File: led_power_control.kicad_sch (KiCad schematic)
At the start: 16 parts, among them Q2001 BSC110N06NS3GATMA1, Q2002 BSC110N06NS3GATMA1, U2001 BD_2EDN8533FXTMA1

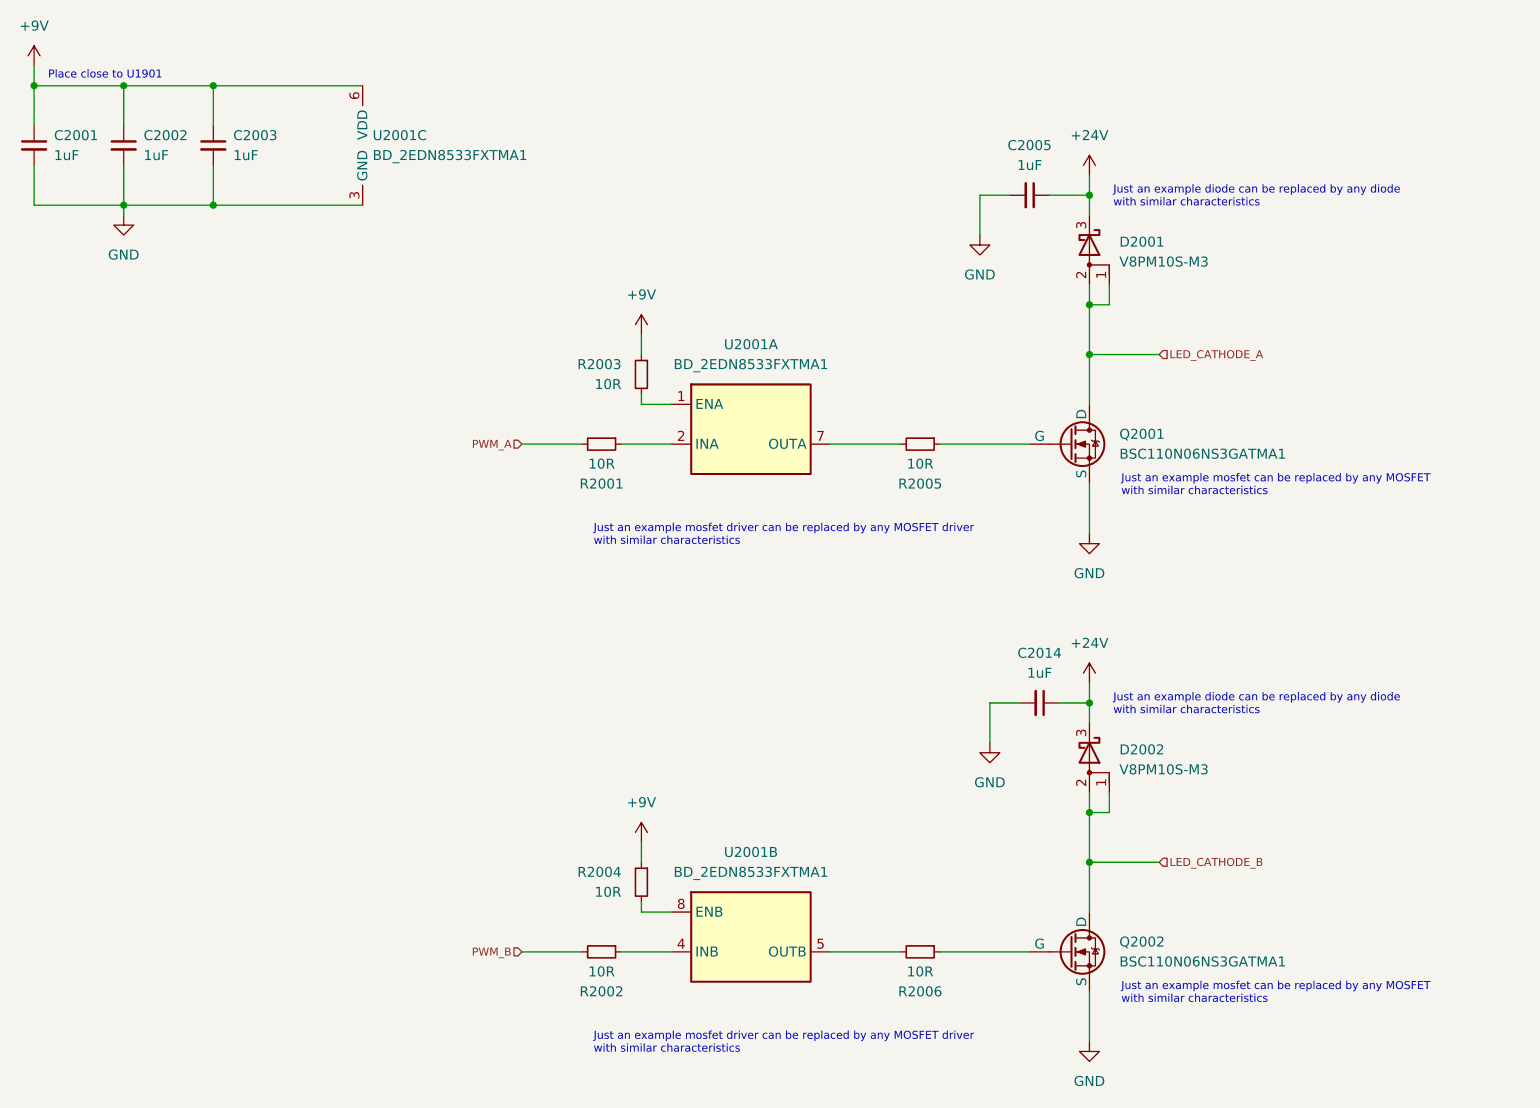
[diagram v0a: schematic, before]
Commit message: Add power supplies
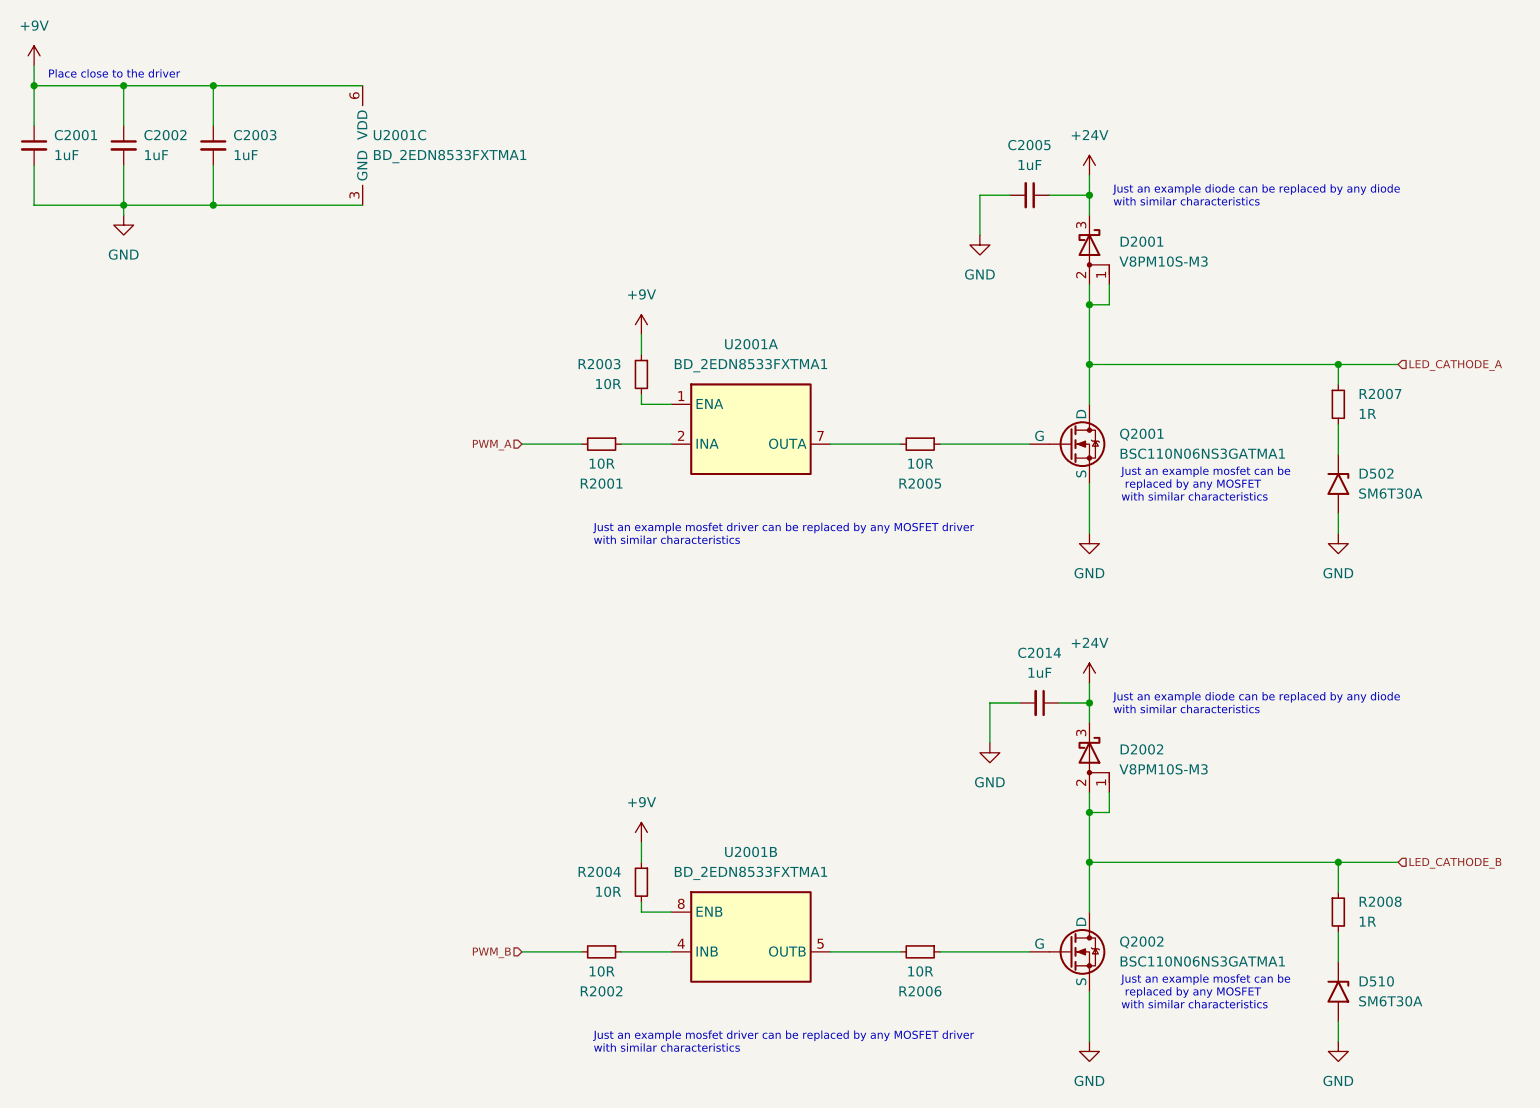
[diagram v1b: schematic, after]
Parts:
- added D502, D510: SM6T30A, Diode_SMD:D_SMB, symbol Diode:SM6T30A
- added R2007, R2008: 1R, symbol Device:R_Small
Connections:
- net GND: now also D502.2 (A2), D510.2 (A2)
- net LED_CATHODE_A: now also R2007.1
- net LED_CATHODE_B: now also R2008.1
- new net: D510.1 (A1), R2008.2
- new net: D502.1 (A1), R2007.2
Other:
- note added: "Place close to the driver"
- note removed: "Place close to U1901"
